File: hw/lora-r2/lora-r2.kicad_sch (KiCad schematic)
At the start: 2 parts, among them U1 Pico_1_PCB

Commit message: Initial layout on LoRa R2
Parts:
- added J1: Conn_Coaxial, symbol Connector:Conn_Coaxial
- added J2: SWD, symbol Connector_Generic:Conn_01x03
- added J3: GPIO, symbol Connector_Generic:Conn_02x08_Top_Bottom
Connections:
- net GND: now also U1.23 (GND), U1.28 (GND), U1.33 (AGND), U1.38 (GND), U1.42 (GND), U2.1 (GND), U2.13 (GND), U2.18 (GND), J1.2 (Ext), J2.2 (Pin_2), J3.16 (Pin_16), J3.8 (Pin_8)
- net SPI_CS: now also U2.7 (NSS)
- net SPI_MISO: now also U2.4 (MISO)
- net SPI_MOSI: now also U2.5 (MOSI)
- net SPI_SCK: now also U2.6 (SCK)
- net at U2.12 (ANT_PAD): now also J1.1 (In)
- net RADIO_BUSY: now reaches U2.14 (BUSY)
- net RADIO_BUSY: now also U1.24 (GPIO18)
- net RADIO_INT: now reaches U2.15 (DIO1)
- net RADIO_INT: now also U1.25 (GPIO19)
- net 3V3_SWITCHED: now reaches U2.2 (VDD)
- net ~{RADIO_RESET}: now reaches U2.3 (~{NRESET})
- net ~{RADIO_RESET}: now also U1.19 (GPIO14)
- net RADIO_RFSW_V2: now reaches U2.8 (RFSW_V2)
- net RADIO_RFSW_V2: now also U1.22 (GPIO17)
- net RADIO_RFSW_V1: now reaches U2.9 (RFSW_V1)
- net RADIO_RFSW_V1: now also U1.21 (GPIO16)
- net GPIO0: now reaches U1.1 (GPIO0)
- net GPIO0: now also J3.1 (Pin_1)
- net GPIO7: now reaches U1.10 (GPIO7)
- net GPIO7: now also J3.10 (Pin_10)
- net GPIO8: now reaches U1.11 (GPIO8)
- net GPIO8: now also J3.11 (Pin_11)
- net GPIO9: now reaches U1.12 (GPIO9)
- net GPIO9: now also J3.12 (Pin_12)
- net GPIO1: now reaches U1.2 (GPIO1)
- net GPIO1: now also J3.2 (Pin_2)
- net GPIO20: now reaches U1.26 (GPIO20)
- net GPIO26: now reaches U1.31 (GPIO26_ADC0)
- net GPIO26: now also J3.14 (Pin_14)
- net GPIO27: now reaches U1.32 (GPIO27_ADC1)
- net GPIO27: now also J3.15 (Pin_15)
- net +3.3V: now reaches U1.39 (VSYS)
- net GPIO2: now reaches U1.4 (GPIO2)
- net GPIO2: now also J3.3 (Pin_3)
- net at U1.41 (SWCLK): now also J2.1 (Pin_1)
- net at U1.43 (SWDIO): now also J2.3 (Pin_3)
- net GPIO3: now reaches U1.5 (GPIO3)
- net GPIO3: now also J3.4 (Pin_4)
- net GPIO4: now reaches U1.6 (GPIO4)
- net GPIO4: now also J3.5 (Pin_5)
- net GPIO5: now reaches U1.7 (GPIO5)
- net GPIO5: now also J3.13 (Pin_13)
- net GPIO6: now reaches U1.9 (GPIO6)
- net GPIO6: now also J3.9 (Pin_9)
- new net VCON_SENSE: J3.7 (Pin_7)
- new net VPAN_SENSE: J3.6 (Pin_6)
- no-connect marks 0 -> 12
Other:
- added sheet Power (power.kicad_sch)
- note added: "Pico has on-board regulator that will run from 3.3V"
- moved on the sheet: U2

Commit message: DRC passing
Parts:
- J1: footprint (none) -> Connector_Coaxial:SMA_Amphenol_132134_Vertical
- J2: footprint (none) -> Connector_PinHeader_2.54mm:PinHeader_1x03_P2.54mm_Vertical
- J3: footprint (none) -> Connector_PinHeader_2.54mm:PinHeader_2x08_P2.54mm_Vertical
- U1: footprint bruce-footprints:RPi_Pico_SMD_TH -> bruce-footprints:RPi_Pico_SMD
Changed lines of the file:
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@@
 			)
 		)
-		(property "Footprint" ""
+		(property "Footprint" "Connector_PinHeader_2.54mm:PinHeader_1x03_P2.54mm_Vertical"
 			(at 102.87 148.59 0)
 			(effects
@@
 			)
 		)
-		(property "Footprint" ""
+		(property "Footprint" "Connector_Coaxial:SMA_Amphenol_132134_Vertical"
 			(at 255.27 48.26 0)
 			(effects
@@
 			)
 		)
-		(property "Footprint" ""
+		(property "Footprint" "Connector_PinHeader_2.54mm:PinHeader_2x08_P2.54mm_Vertical"
 			(at 100.33 171.45 0)
 			(effects
@@
 			)
 		)
-		(property "Footprint" "bruce-footprints:RPi_Pico_SMD_TH"
+		(property "Footprint" "bruce-footprints:RPi_Pico_SMD"
 			(at 102.87 105.41 90)
 			(effects

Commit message: Working on PCB
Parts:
- removed J3: GPIO, Connector_PinHeader_2.54mm:PinHeader_2x08_P2.54mm_Vertical, symbol Connector_Generic:Conn_02x08_Top_Bottom
- added H1, H2, H3, H4: MountingHole, MountingHole:MountingHole_3.5mm, symbol Mechanical:MountingHole
- added J3: Conn_02x08_Odd_Even, Connector_PinHeader_2.54mm:PinHeader_2x08_P2.54mm_Vertical, symbol Connector_Generic:Conn_02x08_Odd_Even
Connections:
- net GND: now also J3.15 (Pin_15), J3.16 (Pin_16)
- net GPIO0: now also J3.1 (Pin_1)
- net GPIO1: now also J3.2 (Pin_2)
- net GPIO2: now also J3.3 (Pin_3)
- net GPIO26: now also J3.12 (Pin_12)
- net GPIO27: now also J3.14 (Pin_14)
- net GPIO3: now also J3.4 (Pin_4)
- net GPIO4: now also J3.5 (Pin_5)
- net GPIO5: now also J3.6 (Pin_6)
- net GPIO6: now also J3.7 (Pin_7)
- net GPIO7: now also J3.8 (Pin_8)
- net GPIO8: now also J3.9 (Pin_9)
- net GPIO9: now also J3.10 (Pin_10)
- net VCON_SENSE: now also J3.13 (Pin_13)
- net VPAN_SENSE: now also J3.11 (Pin_11)

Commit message: Making progress on layout
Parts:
- removed J1: Conn_Coaxial, Connector_Coaxial:SMA_Amphenol_132134_Vertical, symbol Connector:Conn_Coaxial
- removed J2: SWD, Connector_PinHeader_2.54mm:PinHeader_1x03_P2.54mm_Vertical, symbol Connector_Generic:Conn_01x03
- removed J3: Conn_02x08_Odd_Even, Connector_PinHeader_2.54mm:PinHeader_2x08_P2.54mm_Vertical, symbol Connector_Generic:Conn_02x08_Odd_Even
- removed U1: Pico_1_PCB, bruce-footprints:RPi_Pico_SMD, symbol symbol-library-1:Pico_1_PCB
- removed U2: ~, bruce-footprints:RYLR689-LoRa-Module, symbol symbol-library-1:RYLR689_LoRa_Module
- added J3: Conn_02x12_Odd_Even, Connector_PinHeader_2.54mm:PinHeader_2x12_P2.54mm_Vertical, symbol Connector_Generic:Conn_02x12_Odd_Even
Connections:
- net +3.3V: now also J3.7 (Pin_7)
- net GND: now also J3.17 (Pin_17), J3.19 (Pin_19), J3.21 (Pin_21), J3.22 (Pin_22), J3.23 (Pin_23), J3.24 (Pin_24)
- net GPIO0: now also J3.2 (Pin_2)
- net GPIO1: now also J3.4 (Pin_4)
- net GPIO2: now also J3.6 (Pin_6)
- net GPIO26: now also J3.9 (Pin_9)
- net GPIO27: now also J3.13 (Pin_13)
- net GPIO3: now also J3.8 (Pin_8)
- net GPIO4: now also J3.10 (Pin_10)
- net GPIO5: now also J3.12 (Pin_12)
- net GPIO6: now also J3.14 (Pin_14)
- net GPIO7: now also J3.16 (Pin_16)
- net GPIO8: now also J3.18 (Pin_18)
- net GPIO9: now also J3.20 (Pin_20)
- net VCON_SENSE: now also J3.11 (Pin_11)
- net VPAN_SENSE: now also J3.15 (Pin_15)
- new net VCON: J3.5 (Pin_5)
- new net VPAN: J3.1 (Pin_1), J3.3 (Pin_3)
- no-connect marks 12 -> 0
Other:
- added sheet Controller (controller.kicad_sch)
- note removed: "Pico has on-board regulator that will run from 3.3V"
- moved on the sheet: H1, H2, H3, H4

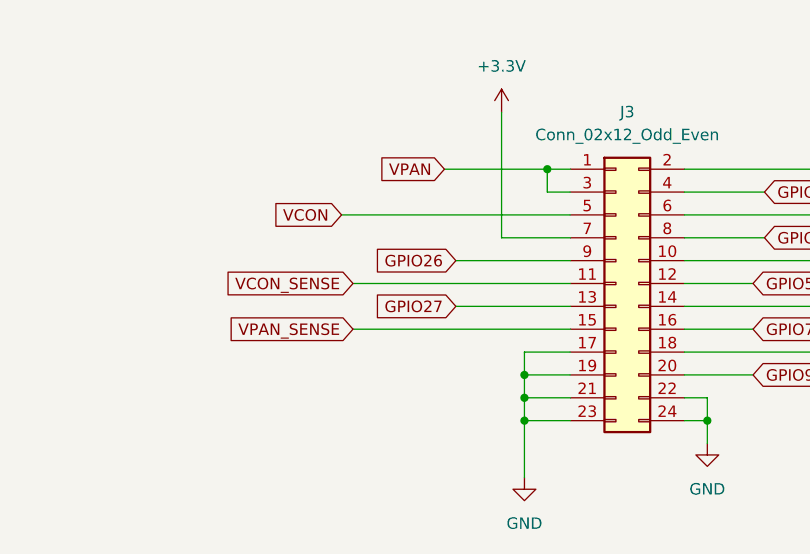
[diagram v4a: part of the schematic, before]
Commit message: First layout that passes DRC
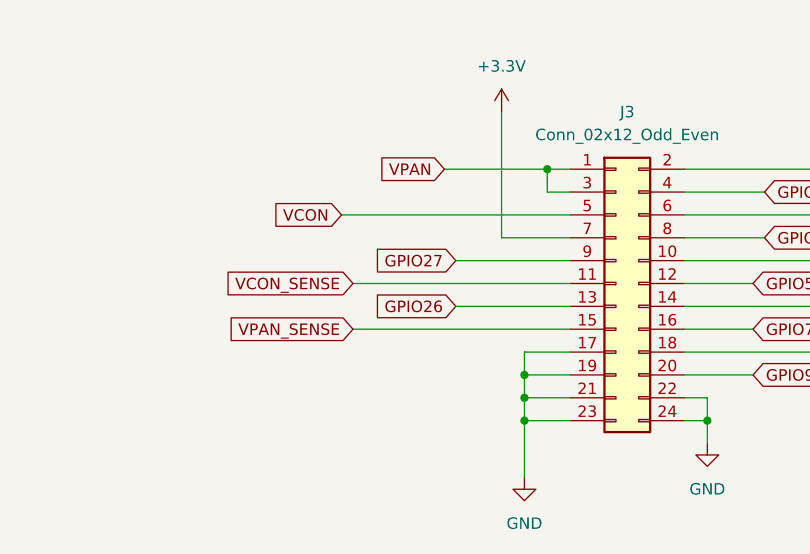
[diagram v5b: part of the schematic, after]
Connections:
- net GPIO26: now also J3.13 (Pin_13); no longer J3.9 (Pin_9)
- net GPIO27: now also J3.9 (Pin_9); no longer J3.13 (Pin_13)
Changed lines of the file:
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@@
 	(global_label "GPIO26"
+		(shape input)
+		(at 80.01 90.17 180)
+		(fields_autoplaced yes)
+		(effects
+			(font
+				(size 1.27 1.27)
+			)
+			(justify right)
+		)
+		(property "Intersheetrefs" "${INTERSHEET_REFS}"
+			(at 70.1305 90.17 0)
+			(effects
+				(font
+					(size 1.27 1.27)
+				)
+				(justify right)
+				(hide yes)
+			)
+		)
+	)
+	(global_label "GPIO27"
 		(shape input)
 		(at 80.01 85.09 180)
@@
 			(effects
 				(font
-					(size 1.27 1.27)
-				)
-				(justify right)
-				(hide yes)
-			)
-		)
-	)
-	(global_label "GPIO27"
-		(shape input)
-		(at 80.01 90.17 180)
-		(fields_autoplaced yes)
-		(effects
-			(font
-				(size 1.27 1.27)
-			)
-			(justify right)
-		)
-		(property "Intersheetrefs" "${INTERSHEET_REFS}"
-			(at 70.1305 90.17 0)
-			(effects
-				(font

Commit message: Generated first Gerbers
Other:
- company: (none) -> Bruce MacKinnon
- title: (none) -> KC1FSZ LoRa Controller Board
- moved on the sheet: H1, H2, H3, H4
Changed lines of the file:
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@@
 	(generator "eeschema")
 	(generator_version "9.0")
-	(paper "A4")
+	(paper "USLetter")
+	(title_block
+		(title "KC1FSZ LoRa Controller Board")
+		(date "2025-05-08")
+		(rev "1")
+		(company "Bruce MacKinnon")
+		(comment 1 "Copyright (C) 2025, Bruce MacKinnon")
+		(comment 2 "NOT FOR COMMERCIAL USE")
+	)
 	(junction
 		(at 107.95 102.87)
@@
 	(symbol
 		(lib_id "Mechanical:MountingHole")
-		(at 261.62 105.41 0)
+		(at 193.04 114.3 0)
 		(unit 1)
 		(exclude_from_sim yes)
@@
 		(fields_autoplaced yes)
 		(property "Reference" "H4"
-			(at 264.16 104.1399 0)
+			(at 195.58 113.0299 0)
 			(effects
 				(font
@@
 		)
 		(property "Value" "MountingHole"
-			(at 264.16 106.6799 0)
+			(at 195.58 115.5699 0)
 			(effects
 				(font
@@
 		)
 		(property "Footprint" "MountingHole:MountingHole_3.5mm"
-			(at 261.62 105.41 0)
+			(at 193.04 114.3 0)
 			(effects
 				(font
@@
 		)
 		(property "Datasheet" "~"
-			(at 261.62 105.41 0)
+			(at 193.04 114.3 0)
 			(effects
 				(font
@@
 		)
 		(property "Description" "Mounting Hole without connection"
-			(at 261.62 105.41 0)
+			(at 193.04 114.3 0)
 			(effects
 				(font
@@
 	(symbol
 		(lib_id "Mechanical:MountingHole")
-		(at 261.62 100.33 0)
+		(at 193.04 109.22 0)
 		(unit 1)
 		(exclude_from_sim yes)
@@
 		(fields_autoplaced yes)
 		(property "Reference" "H3"
-			(at 264.16 99.0599 0)
+			(at 195.58 107.9499 0)
 			(effects
 				(font
@@
 		)
 		(property "Value" "MountingHole"
-			(at 264.16 101.5999 0)
+			(at 195.58 110.4899 0)
 			(effects
 				(font
@@
 		)
 		(property "Footprint" "MountingHole:MountingHole_3.5mm"
-			(at 261.62 100.33 0)
+			(at 193.04 109.22 0)
 			(effects
 				(font
@@
 		)
 		(property "Datasheet" "~"
-			(at 261.62 100.33 0)
+			(at 193.04 109.22 0)
 			(effects
 				(font
@@
 		)
 		(property "Description" "Mounting Hole without connection"
-			(at 261.62 100.33 0)
+			(at 193.04 109.22 0)
 			(effects
 				(font
@@
 	(symbol
 		(lib_id "Mechanical:MountingHole")
-		(at 261.62 95.25 0)
+		(at 193.04 104.14 0)
 		(unit 1)
 		(exclude_from_sim yes)
@@
 		(fields_autoplaced yes)
 		(property "Reference" "H2"
-			(at 264.16 93.9799 0)
+			(at 195.58 102.8699 0)
 			(effects
 				(font
@@
 		)
 		(property "Value" "MountingHole"
-			(at 264.16 96.5199 0)
+			(at 195.58 105.4099 0)
 			(effects
 				(font
@@
 		)
 		(property "Footprint" "MountingHole:MountingHole_3.5mm"
-			(at 261.62 95.25 0)
+			(at 193.04 104.14 0)
 			(effects
 				(font
@@
 		)
 		(property "Datasheet" "~"
-			(at 261.62 95.25 0)
+			(at 193.04 104.14 0)
 			(effects
 				(font
@@
 		)
 		(property "Description" "Mounting Hole without connection"
-			(at 261.62 95.25 0)
+			(at 193.04 104.14 0)
 			(effects
 				(font
@@
 	(symbol
 		(lib_id "Mechanical:MountingHole")
-		(at 261.62 90.17 0)
+		(at 193.04 99.06 0)
 		(unit 1)
 		(exclude_from_sim yes)
@@
 		(fields_autoplaced yes)
 		(property "Reference" "H1"
-			(at 264.16 88.8999 0)
+			(at 195.58 97.7899 0)
 			(effects
 				(font
@@
 		)
 		(property "Value" "MountingHole"
-			(at 264.16 91.4399 0)
+			(at 195.58 100.3299 0)
 			(effects
 				(font
@@
 		)
 		(property "Footprint" "MountingHole:MountingHole_3.5mm"
-			(at 261.62 90.17 0)
+			(at 193.04 99.06 0)
 			(effects
 				(font
@@
 		)
 		(property "Datasheet" "~"
-			(at 261.62 90.17 0)
+			(at 193.04 99.06 0)
 			(effects
 				(font
@@
 		)
 		(property "Description" "Mounting Hole without connection"
-			(at 261.62 90.17 0)
-			(effects
-				(font
+			(at 193.04 99.06 0)
+			(effects
+				(font

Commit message: SENT TO FAB (2025-05-08 13:04)
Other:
- note added: "There are two panel connections so that we can connect one in from the panel and one out to the charge controller."
- note added: "These pins are purposely adjacent so that a jumper block can be used to connect VCON_SENSE and VPAN_SENSE to ADC inputs."
- moved on the sheet: J3
